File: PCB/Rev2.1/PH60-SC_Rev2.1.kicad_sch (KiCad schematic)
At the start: 48 parts, among them J1 USB_C_Receptacle_USB2.0_14P, J3 Conn_01x02_Pin, J4 Conn_01x05_Pin, U1 nRF52840, U5 LIS2DE12, X1 32.768kHz, X2 Crystal_Generic

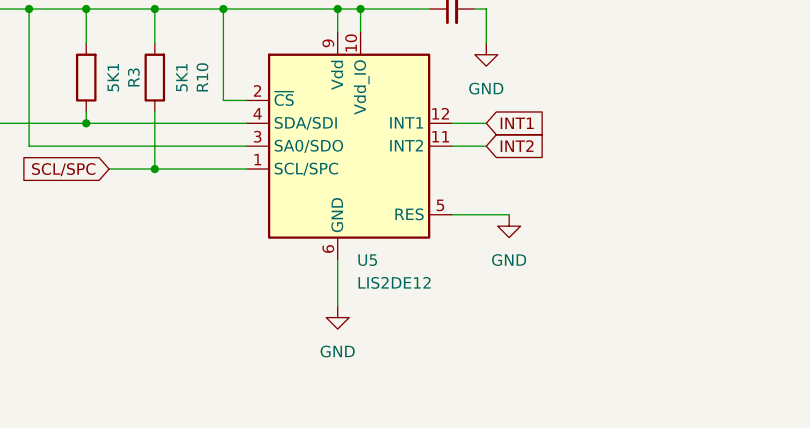
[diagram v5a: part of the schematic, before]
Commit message: 原理图LIS2DE12改为LIS2DH12
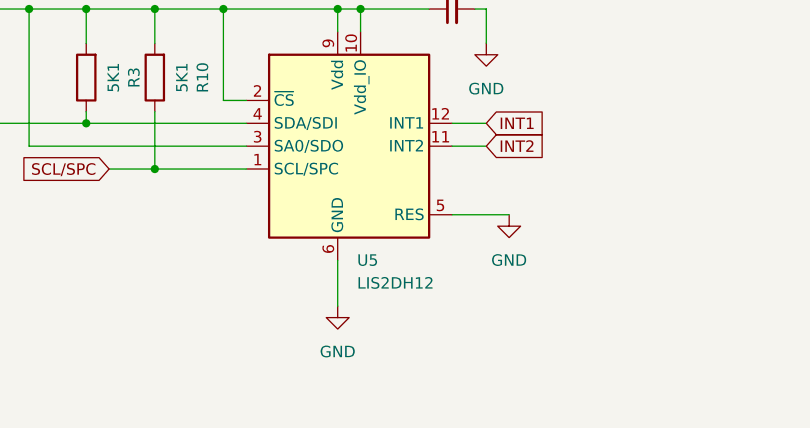
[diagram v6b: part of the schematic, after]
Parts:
- U5: value LIS2DE12 -> LIS2DH12
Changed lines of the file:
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@@
 			)
 		)
-		(property "Value" "LIS2DE12"
+		(property "Value" "LIS2DH12"
 			(at 126.6033 220.98 0)
 			(show_name no)
